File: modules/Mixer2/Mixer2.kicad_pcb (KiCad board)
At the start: 2 copper layers, 91.4 x 108.2 mm, 81 parts, among them J1 WQP-PJ398, J10 Conn_Back_Right_Top, J11 Conn_Front_Right, J12 Conn_Back_Left, J13 Conn_Eurorack_10, J2 WQP-PJ398, J3 WQP-PJ398, J4 WQP-PJ398, J5 WQP-PJ398, J6 WQP-PJ398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

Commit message: Mixer2 - front panel - wip
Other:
- board text added: "TODO: verify positions match Delp panel"
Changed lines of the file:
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@@
+    (effects (font (size 1.016 1.016) (thickness 0.1524)))
+  )
+  (gr_text "TODO: verify positions match Delp panel" (at 120.523 34.163) (layer "Cmts.User")
     (effects (font (size 1.016 1.016) (thickness 0.1524)))
   )

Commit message: Mixer2 - BOM wip
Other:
- board text added: "4 3.2"
- board text added: "5.486614173 3.2"
- board text added: "6.013385827 3.2"
- board text added: "7.5 3.2"
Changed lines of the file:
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@@
+    (effects (font (size 1.016 1.016) (thickness 0.1524)))
+  )
+  (gr_text "6.013385827\n3.2" (at 150.241 80.01) (layer "Cmts.User")
+    (effects (font (size 1.016 1.016) (thickness 0.1524)))
+  )
+  (gr_text "4\n3.2" (at 98.806 80.391) (layer "Cmts.User")
+    (effects (font (size 1.016 1.016) (thickness 0.1524)))
+  )
+  (gr_text "7.5\n3.2" (at 193.675 80.01) (layer "Cmts.User")
     (effects (font (size 1.016 1.016) (thickness 0.1524)))
   )
@@
     (effects (font (size 1.016 1.016) (thickness 0.1524)))
   )
+  (gr_text "5.486614173\n3.2" (at 141.605 79.629) (layer "Cmts.User")
+    (effects (font (size 1.016 1.016) (thickness 0.1524)))
+  )

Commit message: Mixer2 - remove bad diodes
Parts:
- removed the D4 at (185.0, 93.7)
- removed D7: 1N4148, Diode_THT:D_DO-35_SOD27_P7.62mm_Horizontal
- J10: value Conn_Back_Right_Top -> Conn_PCB_Back
- J11: value Conn_Front_Right -> Conn_PCB_Front
- J12: value Conn_Back_Left -> Conn_PCB_Back
- J9: value Conn_Front_Left_Top -> Conn_PCB_Front
- moved R5 26.5 mm to (185.4, 94.9), turned to 90 degrees
- renumbered D5 to D4, D6 to D5, D8 to D6
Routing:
- net GAIN-ATTEN-1: track 45.1 -> 26.2 mm
- net Net-(C10-Pad1): track 12.8 -> 28.8 mm
- net Net-(C11-Pad1): track 69.3 -> 59.4 mm, vias 2 -> 1
- net GAIN-1: track 72.3 -> 70.3 mm
- net OUT-1-NORMAL: track 114.6 -> 112.8 mm
- net IN-ATTEN-1-2: track 49.5 -> 48.2 mm
- net IN-ATTEN-1-3: track 39.3 -> 38.3 mm
- net GAIN-ATTEN-2: track 47.6 -> 48.2 mm

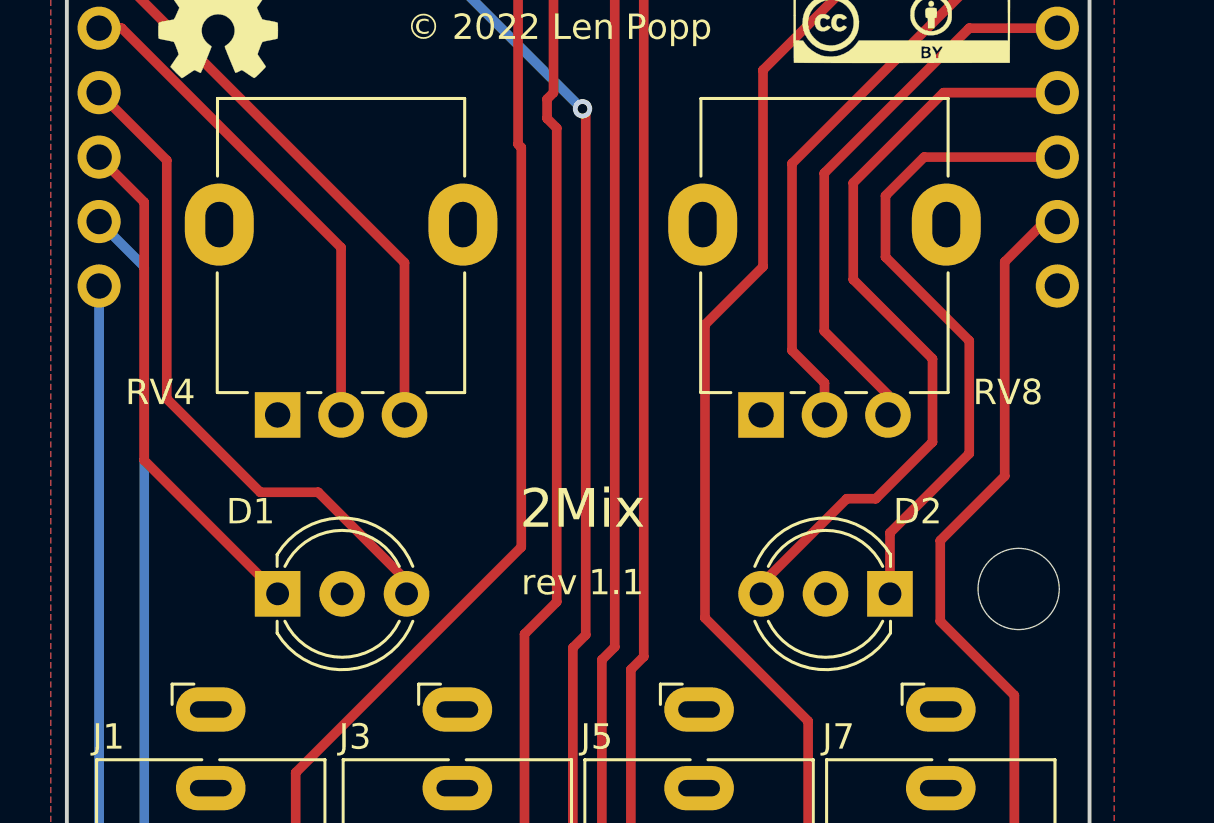
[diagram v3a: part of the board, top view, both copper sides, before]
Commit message: Mixer2 - fix LED positions on PCB
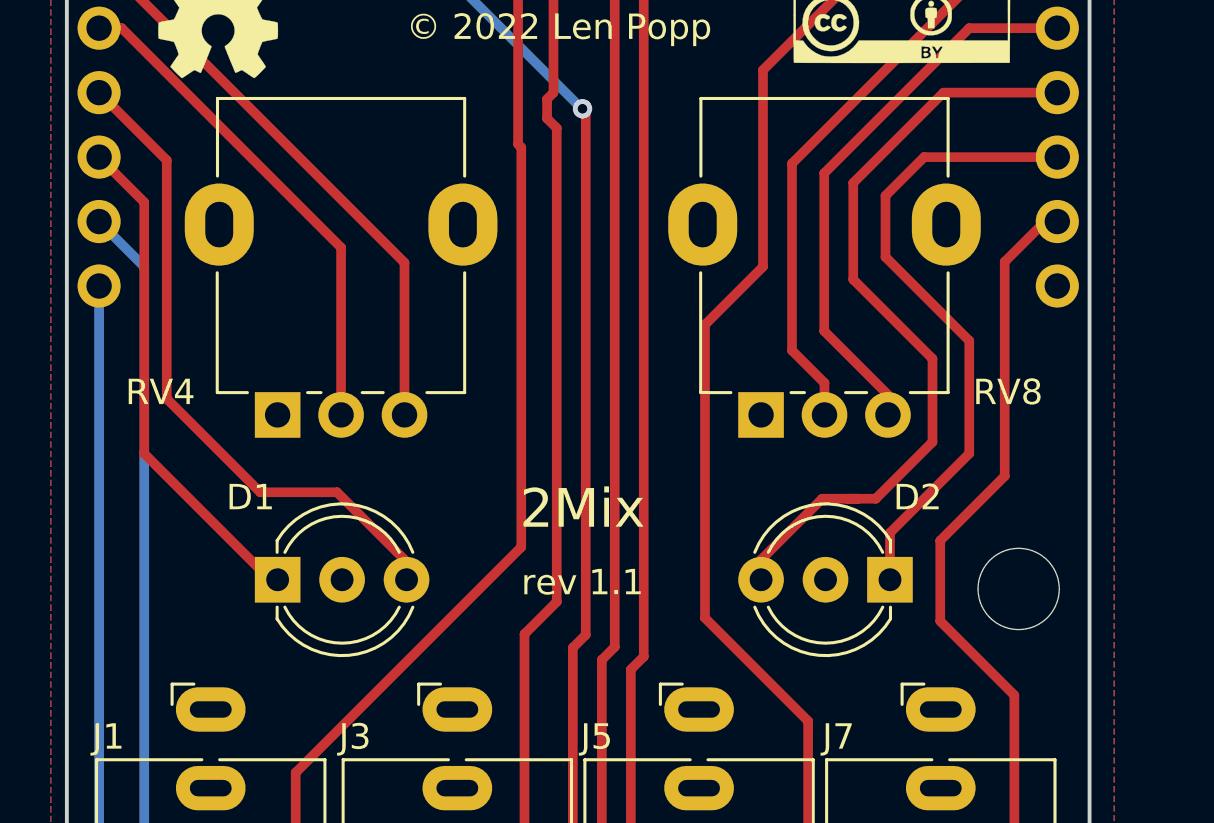
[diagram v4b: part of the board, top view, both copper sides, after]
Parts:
- moved D1 0.56 mm to (108.6, 113.2)
- moved D2 0.56 mm to (132.8, 113.2)
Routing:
- net LED-GREEN-2: track 40.5 -> 41.4 mm
- net LED-RED-2: track 60.7 -> 60.1 mm
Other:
- board text removed: "4 3.2"
- board text removed: "5.486614173 3.2"
- board text removed: "6.013385827 3.2"
- board text removed: "7.5 3.2"
- board text removed: "TODO: verify positions match Delp panel"
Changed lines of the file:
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@@
   )
   (footprint "LED_THT:LED_D5.0mm-3" (layer "F.Cu")
-    (at 132.7658 113.73 180)
+    (at 132.7658 113.175 180)
     (descr "LED, diameter 5.0mm, 2 pins, diameter 5.0mm, 3 pins, http://www.kingbright.com/attachments/file/psearch/000/00/00/L-59EGC(Ver.17A).pdf")
     (tags "LED diameter 5.0mm 2 pins diameter 5.0mm 3 pins")
@@
   )
   (footprint "LED_THT:LED_D5.0mm-3" (layer "F.Cu")
-    (at 108.6358 113.73)
+    (at 108.6358 113.175)
     (descr "LED, diameter 5.0mm, 2 pins, diameter 5.0mm, 3 pins, http://www.kingbright.com/attachments/file/psearch/000/00/00/L-59EGC(Ver.17A).pdf")
     (tags "LED diameter 5.0mm 2 pins diameter 5.0mm 3 pins")
@@
   )
   (gr_text "https://len42.github.io/Synth/" (at 120.523 54.229) (layer "F.SilkS")
-    (effects (font (size 1.016 1.016) (thickness 0.1524)))
-  )
-  (gr_text "6.013385827\n3.2" (at 150.241 80.01) (layer "Cmts.User")
-    (effects (font (size 1.016 1.016) (thickness 0.1524)))
-  )
-  (gr_text "4\n3.2" (at 98.806 80.391) (layer "Cmts.User")
-    (effects (font (size 1.016 1.016) (thickness 0.1524)))
-  )
-  (gr_text "7.5\n3.2" (at 193.675 80.01) (layer "Cmts.User")
-    (effects (font (size 1.016 1.016) (thickness 0.1524)))
-  )
-  (gr_text "TODO: verify positions match Delp panel" (at 120.523 34.163) (layer "Cmts.User")
-    (effects (font (size 1.016 1.016) (thickness 0.1524)))
-  )
-  (gr_text "5.486614173\n3.2" (at 141.605 79.629) (layer "Cmts.User")
     (effects (font (size 1.016 1.016) (thickness 0.1524)))
   )
@@
   (segment (start 166.116 107.046) (end 166.116 102.748) (width 0.381) (layer "B.Cu") (net 14))
   (segment (start 166.116 102.748) (end 167.777 101.087) (width 0.381) (layer "B.Cu") (net 14))
+  (segment (start 108.35 113.175) (end 103.378 108.203) (width 0.381) (layer "F.Cu") (net 15))
+  (segment (start 108.6358 113.175) (end 108.35 113.175) (width 0.381) (layer "F.Cu") (net 15))
+  (segment (start 103.378 108.203) (end 103.378 98.298) (width 0.381) (layer "F.Cu") (net 15))
   (segment (start 103.378 98.298) (end 101.6 96.52) (width 0.381) (layer "F.Cu") (net 15))
   (segment (start 179.558 132.715) (end 179.558 136.271) (width 0.381) (layer "F.Cu") (net 15))
-  (segment (start 108.6358 113.73) (end 103.378 108.4722) (width 0.381) (layer "F.Cu") (net 15))
   (segment (start 190.5 96.52) (end 188.341 98.679) (width 0.381) (layer "F.Cu") (net 15))
-  (segment (start 103.378 108.4722) (end 103.378 98.298) (width 0.381) (layer "F.Cu") (net 15))
   (segment (start 180.086 132.187) (end 180.086 120.015) (width 0.381) (layer "F.Cu") (net 15))
   (segment (start 188.341 98.679) (end 188.341 111.76) (width 0.381) (layer "F.Cu") (net 15))
@@
   (segment (start 189.484 93.98) (end 190.5 93.98) (width 0.381) (layer "F.Cu") (net 16))
   (segment (start 186.563 99.441) (end 185.293 98.171) (width 0.381) (layer "F.Cu") (net 16))
+  (segment (start 104.267 106.045) (end 104.267 96.647) (width 0.381) (layer "F.Cu") (net 16))
+  (segment (start 113.7158 113.175) (end 113.7158 112.4658) (width 0.381) (layer "F.Cu") (net 16))
+  (segment (start 107.95 109.728) (end 104.267 106.045) (width 0.381) (layer "F.Cu") (net 16))
+  (segment (start 110.978 109.728) (end 107.95 109.728) (width 0.381) (layer "F.Cu") (net 16))
+  (segment (start 186.563 110.744) (end 186.563 99.441) (width 0.381) (layer "F.Cu") (net 16))
   (segment (start 104.267 96.647) (end 101.6 93.98) (width 0.381) (layer "F.Cu") (net 16))
-  (segment (start 107.95 109.728) (end 104.267 106.045) (width 0.381) (layer "F.Cu") (net 16))
-  (segment (start 110.236 109.728) (end 107.95 109.728) (width 0.381) (layer "F.Cu") (net 16))
-  (segment (start 104.267 106.045) (end 104.267 96.647) (width 0.381) (layer "F.Cu") (net 16))
-  (segment (start 186.563 110.744) (end 186.563 99.441) (width 0.381) (layer "F.Cu") (net 16))
-  (segment (start 113.7158 113.2078) (end 110.236 109.728) (width 0.381) (layer "F.Cu") (net 16))
   (segment (start 185.293 98.171) (end 189.484 93.98) (width 0.381) (layer "F.Cu") (net 16))
+  (segment (start 113.7158 112.4658) (end 110.978 109.728) (width 0.381) (layer "F.Cu") (net 16))
   (segment (start 137.287 109.093) (end 137.287 100.6475) (width 0.381) (layer "F.Cu") (net 17))
   (segment (start 137.668 140.8335) (end 137.668 117.729) (width 0.381) (layer "F.Cu") (net 17))
@@
   (segment (start 160.274 92.583) (end 160.274 97.282) (width 0.381) (layer "B.Cu") (net 17))
   (segment (start 153.248 99.568) (end 157.988 99.568) (width 0.381) (layer "B.Cu") (net 17))
-  (segment (start 139.36 96.52) (end 134.112 96.52) (width 0.381) (layer "F.Cu") (net 18))
-  (segment (start 132.7658 111.3282) (end 132.7658 113.73) (width 0.381) (layer "F.Cu") (net 18))
-  (segment (start 134.112 96.52) (end 132.588 98.044) (width 0.381) (layer "F.Cu") (net 18))
+  (segment (start 135.89 108.204) (end 135.89 103.759) (width 0.381) (layer "F.Cu") (net 18))
+  (segment (start 132.588 100.457) (end 132.588 98.044) (width 0.381) (layer "F.Cu") (net 18))
   (segment (start 156.21 110.49) (end 157.968 112.248) (width 0.381) (layer "F.Cu") (net 18))
   (segment (start 156.21 106.553) (end 156.21 99.695) (width 0.381) (layer "F.Cu") (net 18))
-  (segment (start 135.89 103.759) (end 135.89 108.204) (width 0.381) (layer "F.Cu") (net 18))
+  (segment (start 132.588 98.044) (end 134.112 96.52) (width 0.381) (layer "F.Cu") (net 18))
+  (segment (start 132.7658 113.175) (end 132.7658 111.3282) (width 0.381) (layer "F.Cu") (net 18))
+  (segment (start 135.89 103.759) (end 132.588 100.457) (width 0.381) (layer "F.Cu") (net 18))
+  (segment (start 132.7658 111.3282) (end 135.89 108.204) (width 0.381) (layer "F.Cu") (net 18))
   (segment (start 157.968 126.111) (end 154.666 126.111) (width 0.381) (layer "F.Cu") (net 18))
-  (segment (start 132.588 98.044) (end 132.588 100.457) (width 0.381) (layer "F.Cu") (net 18))
+  (segment (start 134.112 96.52) (end 139.36 96.52) (width 0.381) (layer "F.Cu") (net 18))
   (segment (start 156.21 106.553) (end 156.21 110.49) (width 0.381) (layer "F.Cu") (net 18))
   (segment (start 157.968 112.248) (end 157.968 126.111) (width 0.381) (layer "F.Cu") (net 18))
-  (segment (start 135.89 108.204) (end 132.7658 111.3282) (width 0.381) (layer "F.Cu") (net 18))
-  (segment (start 132.588 100.457) (end 135.89 103.759) (width 0.381) (layer "F.Cu") (net 18))
   (segment (start 156.21 99.695) (end 153.035 96.52) (width 0.381) (layer "F.Cu") (net 18))
   (segment (start 131.064 109.982) (end 132.207 109.982) (width 0.381) (layer "F.Cu") (net 19))
   (segment (start 131.318 97.536) (end 134.874 93.98) (width 0.381) (layer "F.Cu") (net 19))
+  (segment (start 127.6858 112.3892) (end 130.093 109.982) (width 0.381) (layer "F.Cu") (net 19))
   (segment (start 134.442005 104.470005) (end 131.318 101.346) (width 0.381) (layer "F.Cu") (net 19))
   (segment (start 134.874 93.98) (end 139.36 93.98) (width 0.381) (layer "F.Cu") (net 19))
+  (segment (start 130.093 109.982) (end 131.532 109.982) (width 0.381) (layer "F.Cu") (net 19))
   (segment (start 157.988 101.981) (end 157.988 98.806) (width 0.381) (layer "F.Cu") (net 19))
   (segment (start 131.318 101.346) (end 131.318 97.536) (width 0.381) (layer "F.Cu") (net 19))
@@
   (segment (start 132.207 109.982) (end 134.442005 107.746995) (width 0.381) (layer "F.Cu") (net 19))
   (segment (start 153.162 93.98) (end 152.74 93.98) (width 0.381) (layer "F.Cu") (net 19))
-  (segment (start 127.6858 113.3602) (end 131.064 109.982) (width 0.381) (layer "F.Cu") (net 19))
+  (segment (start 127.6858 113.175) (end 127.6858 112.3892) (width 0.381) (layer "F.Cu") (net 19))
   (segment (start 118.237 82.423) (end 118.237 54.1312) (width 0.381) (layer "F.Cu") (net 20))
   (segment (start 109.347 120.777) (end 118.237 111.887) (width 0.381) (layer "F.Cu") (net 20))

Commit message: Mixer2 - PCB update - wip
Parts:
- D3, D5: value 1N4148 -> 1N5711
- moved R24 7.64 mm to (161.0, 117.7), turned to 0 degrees
- moved R25 7.62 mm to (168.6, 121.4), turned to 180 degrees
- moved D3 7.62 mm to (174.9, 80.4), turned to -90 degrees
- moved D5 7.62 mm to (169.0, 71.5), turned to -90 degrees
- moved R27 7.62 mm to (182.9, 120.4), turned to 180 degrees
- moved R26 7.58 mm to (174.2, 125.0), turned to 180 degrees
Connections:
- D3 pad 1: Net-(C11-Pad1) -> GAIN-1
- D3 pad 2: Net-(C10-Pad2) -> Net-(C11-Pad1)
- D5 pad 1: Net-(C14-Pad1) -> GAIN-2
- D5 pad 2: Net-(C13-Pad2) -> Net-(C14-Pad1)
- R24 pad 1: +12V -> VREF-5
- R24 pad 2: VREF-5 -> -12V
- R25 pad 1: VREF-5 -> VREF-4
- R25 pad 2: VREF-4 -> VREF-5
- R26 pad 1: VREF-4 -> VREF-LO
- R26 pad 2: VREF-LO -> VREF-4
- R27 pad 1: VREF-LO -> GND
- R27 pad 2: GND -> VREF-LO
- U2 pad 10: VREF-5 -> Net-(C11-Pad1)
- U2 pad 12: Net-(C11-Pad1) -> VREF-LO
- U2 pad 13: VREF-LO -> Net-(C11-Pad1)
- U2 pad 2: Net-(C14-Pad1) -> VREF-5
- U2 pad 3: VREF-5 -> Net-(C14-Pad1)
- U2 pad 5: Net-(C14-Pad1) -> VREF-LO
- U2 pad 6: VREF-LO -> Net-(C14-Pad1)
- U2 pad 9: Net-(C11-Pad1) -> VREF-5
- U3 pad 2: VREF-4 -> Net-(C11-Pad1)
- U3 pad 3: Net-(C11-Pad1) -> VREF-4
- U3 pad 5: Net-(C14-Pad1) -> VREF-4
- U3 pad 6: VREF-4 -> Net-(C14-Pad1)
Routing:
- net Net-(C14-Pad1): track 65.3 -> 16.3 mm
- net Net-(C11-Pad1): track 59.4 -> 15.8 mm, vias 1 -> 0
- net VREF-5: track 35.0 -> 0.00 mm
- net VREF-LO: track 45.5 -> 29.4 mm
- net VREF-4: track 21.4 -> 12.3 mm
- net +12V: track 141.0 -> 132.7 mm
- net Net-(C10-Pad2): track 28.6 -> 22.3 mm
- net Net-(C13-Pad2): track 20.8 -> 15.2 mm

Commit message: Mixer2 - PCB update - done
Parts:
- moved D5 10.7 mm to (161.3, 79.0), turned to 0 degrees
- moved D3 3.30 mm to (178.2, 80.4)
- moved R8 3.30 mm to (174.9, 80.4)
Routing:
- net Net-(C11-Pad1): track 15.8 -> 64.8 mm, vias 0 -> 1
- net Net-(C14-Pad1): track 16.3 -> 62.1 mm
- net VREF-5: track 0.00 -> 41.3 mm
- net GAIN-1: track 70.3 -> 89.2 mm
- net VREF-LO: track 29.4 -> 38.2 mm
- net VREF-4: track 12.3 -> 18.3 mm
- net -12V: track 145.4 -> 149.2 mm, vias 2 -> 3
- net Net-(C13-Pad2): track 15.2 -> 18.6 mm
- net GAIN-2: track 71.7 -> 74.1 mm
- net Net-(C10-Pad2): track 22.3 -> 19.9 mm
